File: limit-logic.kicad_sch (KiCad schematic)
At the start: 51 parts, among them U801 4078, U802 4043, U803 4043

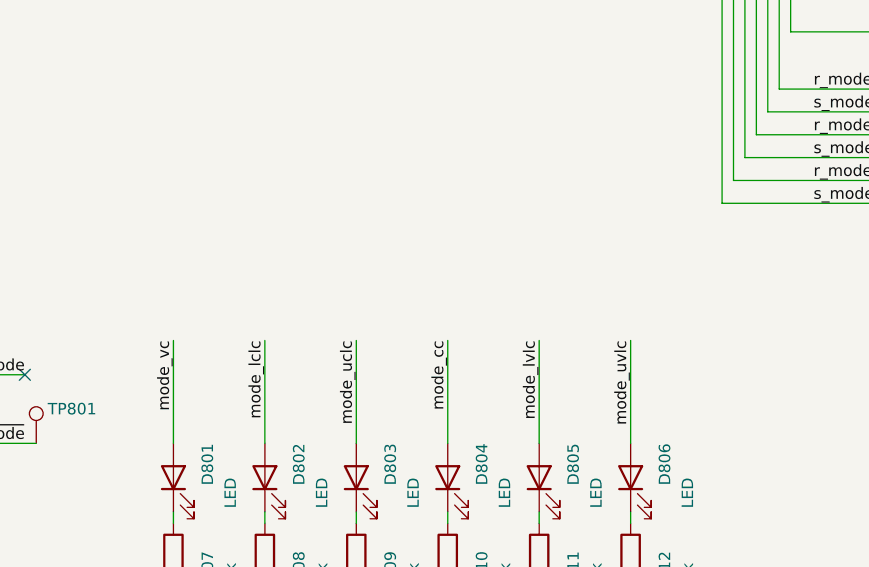
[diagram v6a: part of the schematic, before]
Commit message: add pss lightpipe to schematic
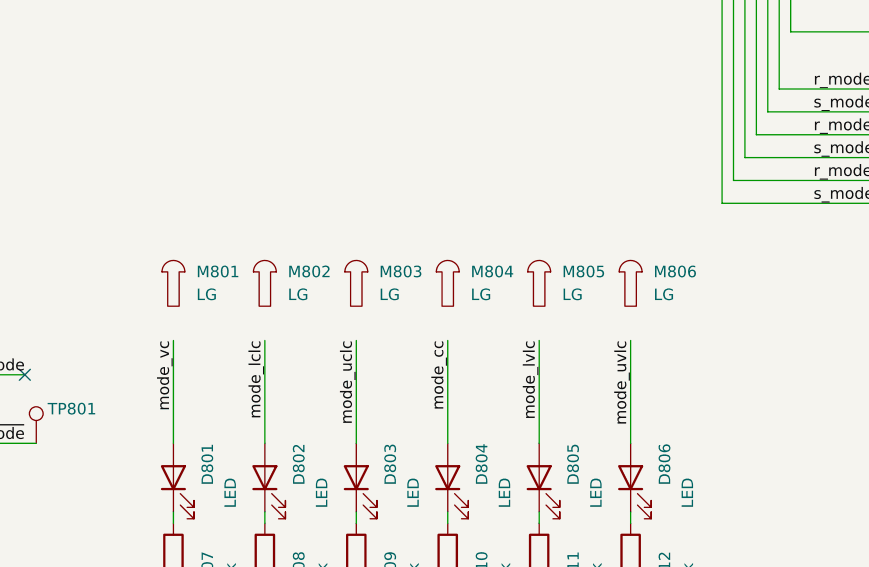
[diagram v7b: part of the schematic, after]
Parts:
- added M801, M802, M803, M804, M805, M806: LG, symbol pss:Lightguide_D4mm_L22.86mm_Dout5mm

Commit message: fix pss lightpipe length variant selection
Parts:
- M801, M802, M803, M804, M805, M806: MPN 51513510900F -> 51513510188F; VPN 645-51513510900F -> 645-51513510188F
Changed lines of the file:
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@@
 			)
 		)
-		(property "MPN" "51513510900F"
+		(property "MPN" "51513510188F"
 			(at 163.83 151.13 0)
 			(effects
@@
 			)
 		)
-		(property "VPN" "645-51513510900F"
+		(property "VPN" "645-51513510188F"
 			(at 163.83 151.13 0)
 			(effects
@@
 			)
 		)
-		(property "MPN" "51513510900F"
+		(property "MPN" "51513510188F"
 			(at 113.03 151.13 0)
 			(effects
@@
 			)
 		)
-		(property "VPN" "645-51513510900F"
+		(property "VPN" "645-51513510188F"
 			(at 113.03 151.13 0)
 			(effects
@@
 			)
 		)
-		(property "MPN" "51513510900F"
+		(property "MPN" "51513510188F"
 			(at 153.67 151.13 0)
 			(effects
@@
 			)
 		)
-		(property "VPN" "645-51513510900F"
+		(property "VPN" "645-51513510188F"
 			(at 153.67 151.13 0)
 			(effects
@@
 			)
 		)
-		(property "MPN" "51513510900F"
+		(property "MPN" "51513510188F"
 			(at 123.19 151.13 0)
 			(effects
@@
 			)
 		)
-		(property "VPN" "645-51513510900F"
+		(property "VPN" "645-51513510188F"
 			(at 123.19 151.13 0)
 			(effects
@@
 			)
 		)
-		(property "MPN" "51513510900F"
+		(property "MPN" "51513510188F"
 			(at 133.35 151.13 0)
 			(effects
@@
 			)
 		)
-		(property "VPN" "645-51513510900F"
+		(property "VPN" "645-51513510188F"
 			(at 133.35 151.13 0)
 			(effects
@@
 			)
 		)
-		(property "MPN" "51513510900F"
+		(property "MPN" "51513510188F"
 			(at 143.51 151.13 0)
 			(effects
@@
 			)
 		)
-		(property "VPN" "645-51513510900F"
+		(property "VPN" "645-51513510188F"
 			(at 143.51 151.13 0)
 			(effects
